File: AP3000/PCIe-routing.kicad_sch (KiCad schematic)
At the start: 15 parts, among them J12 Bus_PCI_Express_Mini

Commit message: Finished routing board.
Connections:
- net PCIE_RX_N: now also J12.25 (PERp0); no longer J12.23 (PERn0)
- net PCIE_RX_P: now also J12.23 (PERn0); no longer J12.25 (PERp0)
- net PCIE_TX_N: now also J12.33 (PETp0); no longer J12.31 (PETn0)
- net PCIE_TX_P: now also J12.31 (PETn0); no longer J12.33 (PETp0)
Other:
- note added: "Note: Polarity inversion on data lanes"
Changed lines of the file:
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@@
   (junction (at 208.28 83.185) (diameter 1.016) (color 0 0 0 0))
   (junction (at 208.28 93.98) (diameter 1.016) (color 0 0 0 0))
-  (no_connect (at 168.275 70.485))
   (no_connect (at 168.275 106.045))
+  (no_connect (at 168.275 108.585))
+  (no_connect (at 168.275 78.105))
+  (no_connect (at 168.275 95.885))
+  (no_connect (at 132.715 108.585))
+  (no_connect (at 132.715 98.425))
+  (no_connect (at 168.275 103.505))
+  (no_connect (at 132.715 67.945))
   (no_connect (at 132.715 70.485))
-  (no_connect (at 168.275 111.125))
-  (no_connect (at 132.715 95.885))
-  (no_connect (at 132.715 98.425))
-  (no_connect (at 168.275 65.405))
-  (no_connect (at 168.275 67.945))
-  (no_connect (at 132.715 67.945))
-  (no_connect (at 168.275 108.585))
   (no_connect (at 168.275 100.965))
   (no_connect (at 168.275 98.425))
-  (no_connect (at 168.275 103.505))
+  (no_connect (at 168.275 111.125))
+  (no_connect (at 168.275 67.945))
+  (no_connect (at 168.275 65.405))
+  (no_connect (at 132.715 95.885))
   (no_connect (at 168.275 75.565))
-  (no_connect (at 168.275 95.885))
-  (no_connect (at 132.715 108.585))
-  (no_connect (at 168.275 78.105))
+  (no_connect (at 168.275 70.485))
   (wire (pts (xy 69.215 45.085) (xy 69.215 47.625))
     (stroke (width 0) (type solid) (color 0 0 0 0))
@@
   (wire (pts (xy 215.9 93.98) (xy 208.28 93.98))
     (stroke (width 0) (type solid) (color 0 0 0 0))
+  )
+  (text "Note: Polarity inversion on data lanes" (at 127.635 73.025 180)
+    (effects (font (size 1.27 1.27)) (justify right bottom))
   )
   (text "Mini PCI Express" (at 167.005 36.195 180)
@@
     (effects (font (size 1.27 1.27)) (justify right))
   )
-  (hierarchical_label "PCIE_TX_P" (shape input) (at 118.11 75.565 180)
-    (effects (font (size 1.27 1.27)) (justify right))
-  )
-  (hierarchical_label "PCIE_TX_N" (shape input) (at 118.11 78.105 180)
-    (effects (font (size 1.27 1.27)) (justify right))
-  )
-  (hierarchical_label "PCIE_RX_P" (shape output) (at 118.11 80.645 180)
-    (effects (font (size 1.27 1.27)) (justify right))
-  )
-  (hierarchical_label "PCIE_RX_N" (shape output) (at 118.11 83.185 180)
-    (effects (font (size 1.27 1.27)) (justify right))
-  )
+  (hierarchical_label "PCIE_TX_N" (shape input) (at 118.11 75.565 180)
+    (effects (font (size 1.27 1.27)) (justify right))
+  )
+  (hierarchical_label "PCIE_TX_P" (shape input) (at 118.11 78.105 180)
+    (effects (font (size 1.27 1.27)) (justify right))
+  )
+  (hierarchical_label "PCIE_RX_N" (shape output) (at 118.11 80.645 180)
+    (effects (font (size 1.27 1.27)) (justify right))
+  )
+  (hierarchical_label "PCIE_RX_P" (shape output) (at 118.11 83.185 180)
+    (effects (font (size 1.27 1.27)) (justify right))
+  )

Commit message: AP3000: Fixup PartsBoxID linkage and placed first order Working on a design for a 5 GHz panel antenna array for a point-to-point replacement
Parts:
- C41, C42: PartsBoxID 1206-100uF-X5R-6.3V -> 1206-47uF-X5R-10V
- JP1: PartsBoxID (none) -> C124374
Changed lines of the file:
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@@
   (junction (at 208.28 83.185) (diameter 1.016) (color 0 0 0 0))
   (junction (at 208.28 93.98) (diameter 1.016) (color 0 0 0 0))
+  (no_connect (at 168.275 67.945))
+  (no_connect (at 168.275 70.485))
+  (no_connect (at 132.715 70.485))
+  (no_connect (at 168.275 78.105))
+  (no_connect (at 132.715 95.885))
+  (no_connect (at 168.275 75.565))
+  (no_connect (at 168.275 95.885))
+  (no_connect (at 168.275 108.585))
+  (no_connect (at 168.275 103.505))
+  (no_connect (at 168.275 111.125))
   (no_connect (at 168.275 106.045))
-  (no_connect (at 168.275 108.585))
-  (no_connect (at 168.275 78.105))
-  (no_connect (at 168.275 95.885))
   (no_connect (at 132.715 108.585))
-  (no_connect (at 132.715 98.425))
-  (no_connect (at 168.275 103.505))
+  (no_connect (at 168.275 65.405))
   (no_connect (at 132.715 67.945))
-  (no_connect (at 132.715 70.485))
   (no_connect (at 168.275 100.965))
   (no_connect (at 168.275 98.425))
-  (no_connect (at 168.275 111.125))
-  (no_connect (at 168.275 67.945))
-  (no_connect (at 168.275 65.405))
-  (no_connect (at 132.715 95.885))
-  (no_connect (at 168.275 75.565))
-  (no_connect (at 168.275 70.485))
+  (no_connect (at 132.715 98.425))
   (wire (pts (xy 69.215 45.085) (xy 69.215 47.625))
     (stroke (width 0) (type solid) (color 0 0 0 0))
@@
       (effects (font (size 1.27 1.27)) hide)
     )
+    (property "PartsBoxID" "C124374" (id 4) (at 184.785 83.185 0)
+      (effects (font (size 1.27 1.27)) hide)
+    )
   )
   (symbol (lib_id "Device:C") (at 69.215 53.34 0) (unit 1)
@@
       (effects (font (size 1.27 1.27)) hide)
     )
-    (property "PartsBoxID" "1206-100uF-X5R-6.3V" (id 4) (at 191.77 88.265 0)
+    (property "PartsBoxID" "1206-47uF-X5R-10V" (id 4) (at 191.77 88.265 0)
       (effects (font (size 1.27 1.27)) hide)
     )
@@
       (effects (font (size 1.27 1.27)) hide)
     )
-    (property "PartsBoxID" "1206-100uF-X5R-6.3V" (id 4) (at 200.66 88.265 0)
-      (effects (font (size 1.27 1.27)) hide)
-    )
+    (property "PartsBoxID" "1206-47uF-X5R-10V" (id 4) (at 200.66 88.265 0)
+      (effects (font (size 1.27 1.27)) hide)
+    )

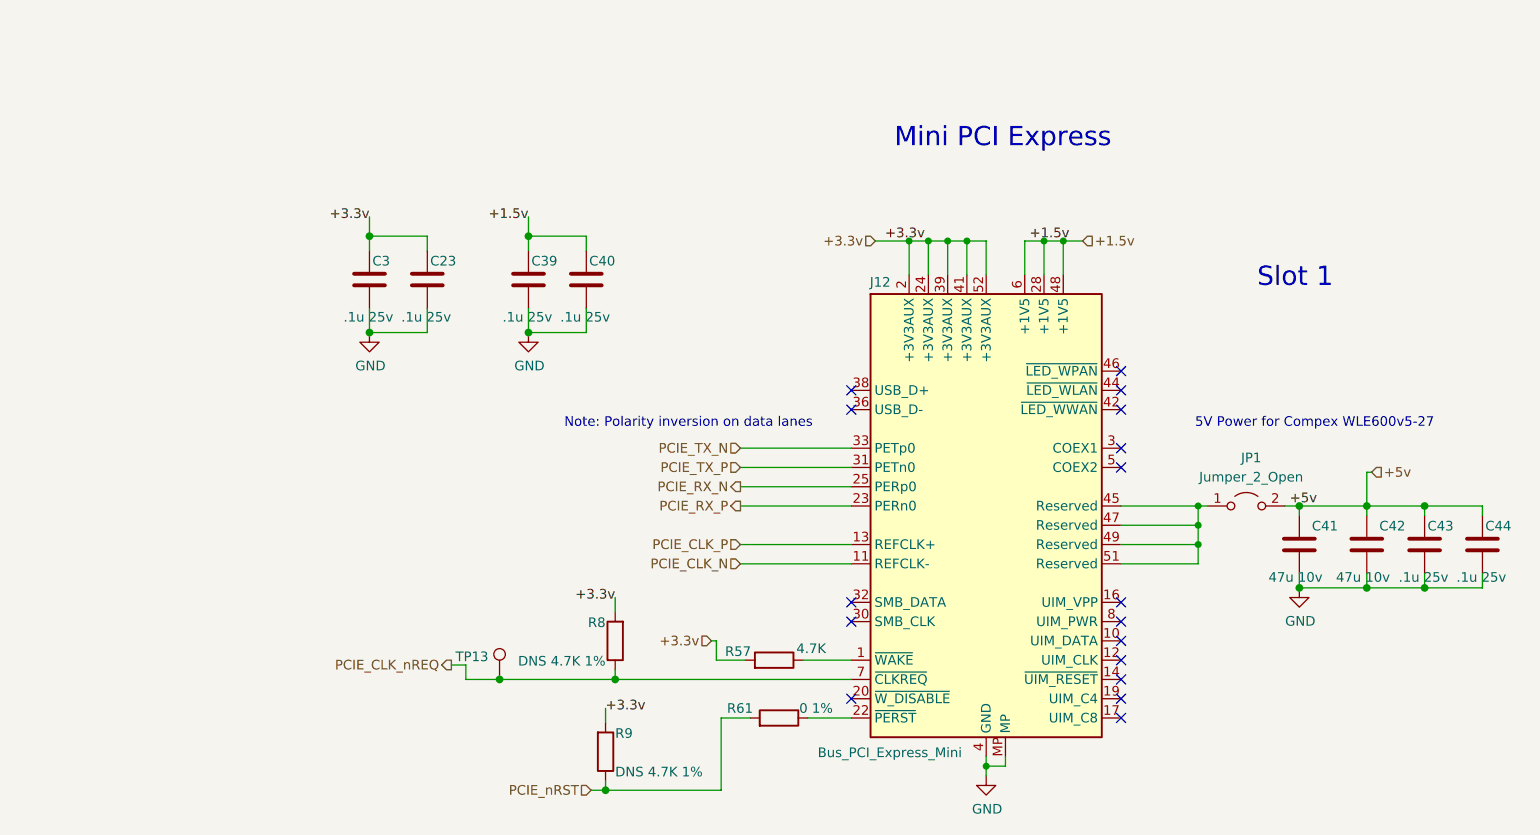
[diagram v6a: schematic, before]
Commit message: Rework AP3000 PoE section, power section and change solder paste to -10% overall, -15% for small chips / mpcie and -20% for the raspi connector
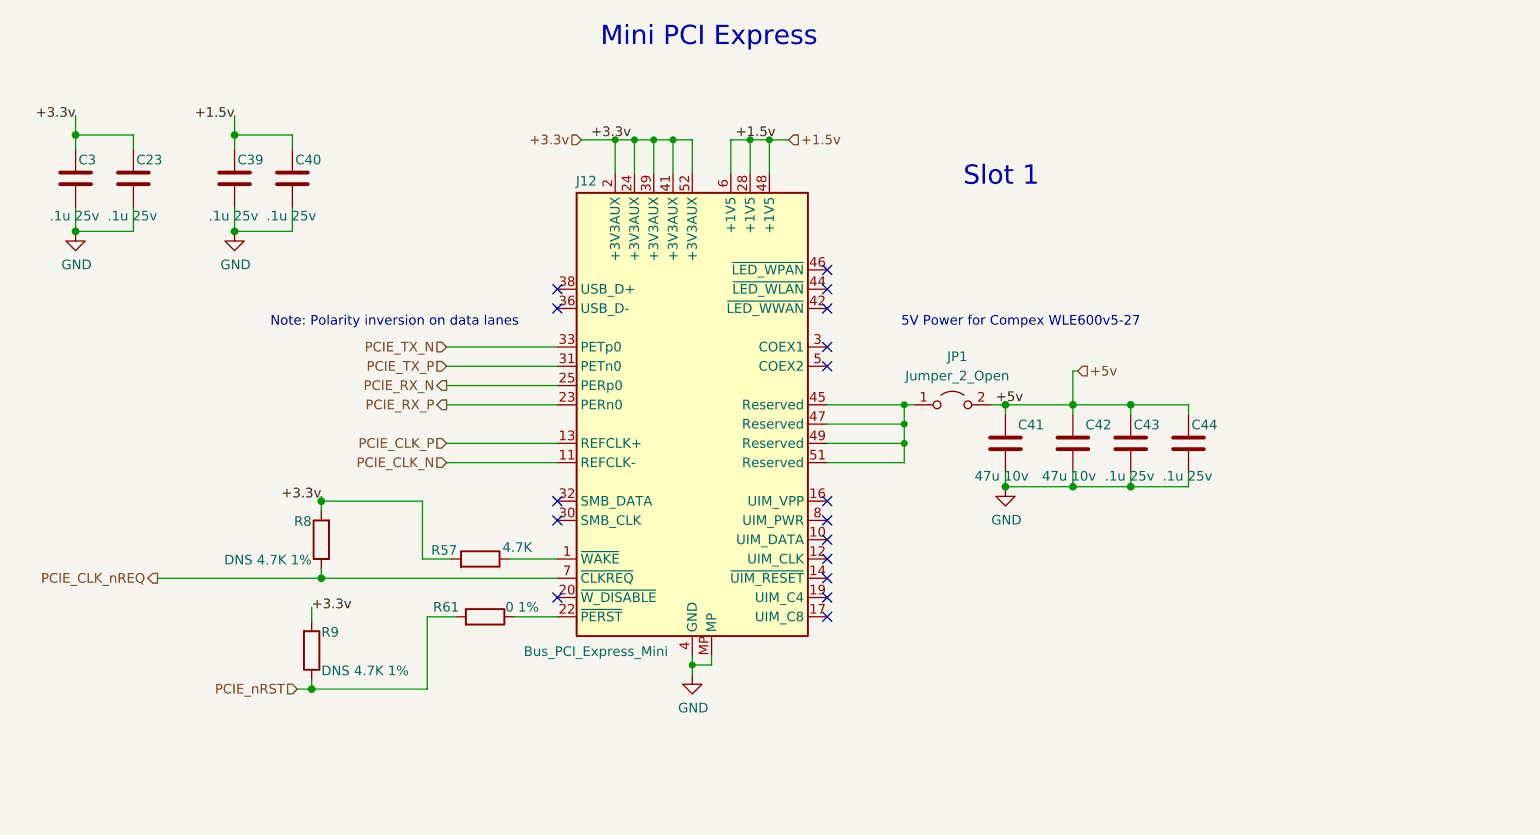
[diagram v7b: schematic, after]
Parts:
- removed TP13: TestPoint, TestPoint:TestPoint_Pad_2.0x2.0mm, symbol Connector:TestPoint
- C23, C3, C39, C40, C43, C44: footprint Capacitor_SMD:C_0402_1005Metric -> Capacitor_SMD:C_0603_1608Metric; PartsBoxID 0402-100nF-X7R-25V -> 0603-100nF-X7R-25V
- R57, R8, R9: footprint Resistor_SMD:R_0402_1005Metric -> Resistor_SMD:R_0603_1608Metric; PartsBoxID 0402-4.7K-1% -> 0603-4.7K-1%
- R61: footprint Resistor_SMD:R_0402_1005Metric -> Resistor_SMD:R_0603_1608Metric; PartsBoxID 0402-0-1% -> 0603-0-1%
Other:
- moved on the sheet: C23, C3, C39, C40, C41, C42, C43, C44, J12, JP1, R57, R61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

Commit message: Ordered AP3000 PCBs Ordered FlatAntPanel4x4 PCBs Ordered FlatAntPanel4x4_Reflector PCBs
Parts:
- R61: PartsBoxID 0603-0-1% -> 0603-0R-1%
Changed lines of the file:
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@@
   (junction (at 169.545 69.85) (diameter 1.016) (color 0 0 0 0))
   (junction (at 169.545 80.645) (diameter 1.016) (color 0 0 0 0))
+  (no_connect (at 93.98 82.55))
+  (no_connect (at 93.98 54.61))
+  (no_connect (at 93.98 95.25))
+  (no_connect (at 129.54 95.25))
+  (no_connect (at 129.54 85.09))
+  (no_connect (at 129.54 97.79))
+  (no_connect (at 129.54 54.61))
+  (no_connect (at 129.54 64.77))
+  (no_connect (at 93.98 85.09))
+  (no_connect (at 129.54 87.63))
+  (no_connect (at 129.54 52.07))
+  (no_connect (at 129.54 90.17))
   (no_connect (at 129.54 57.15))
-  (no_connect (at 129.54 54.61))
-  (no_connect (at 129.54 85.09))
+  (no_connect (at 129.54 62.23))
+  (no_connect (at 129.54 92.71))
   (no_connect (at 93.98 57.15))
-  (no_connect (at 93.98 95.25))
-  (no_connect (at 129.54 92.71))
-  (no_connect (at 129.54 95.25))
-  (no_connect (at 93.98 54.61))
   (no_connect (at 129.54 82.55))
-  (no_connect (at 129.54 97.79))
-  (no_connect (at 93.98 82.55))
-  (no_connect (at 129.54 87.63))
-  (no_connect (at 129.54 90.17))
-  (no_connect (at 93.98 85.09))
-  (no_connect (at 129.54 62.23))
-  (no_connect (at 129.54 52.07))
-  (no_connect (at 129.54 64.77))
   (wire (pts (xy 30.48 31.75) (xy 30.48 34.29))
     (stroke (width 0) (type solid) (color 0 0 0 0))
@@
       (effects (font (size 1.27 1.27)) hide)
     )
-    (property "PartsBoxID" "0603-0-1%" (id 4) (at 84.455 97.79 0)
-      (effects (font (size 1.27 1.27)) hide)
-    )
+    (property "PartsBoxID" "0603-0R-1%" (id 4) (at 84.455 97.79 0)
+      (effects (font (size 1.27 1.27)) hide)
+    )
